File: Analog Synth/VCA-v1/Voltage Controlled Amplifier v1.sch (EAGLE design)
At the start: 40 parts, among them IC2 TL084P, IC3 TL084P, IC4 CA3046

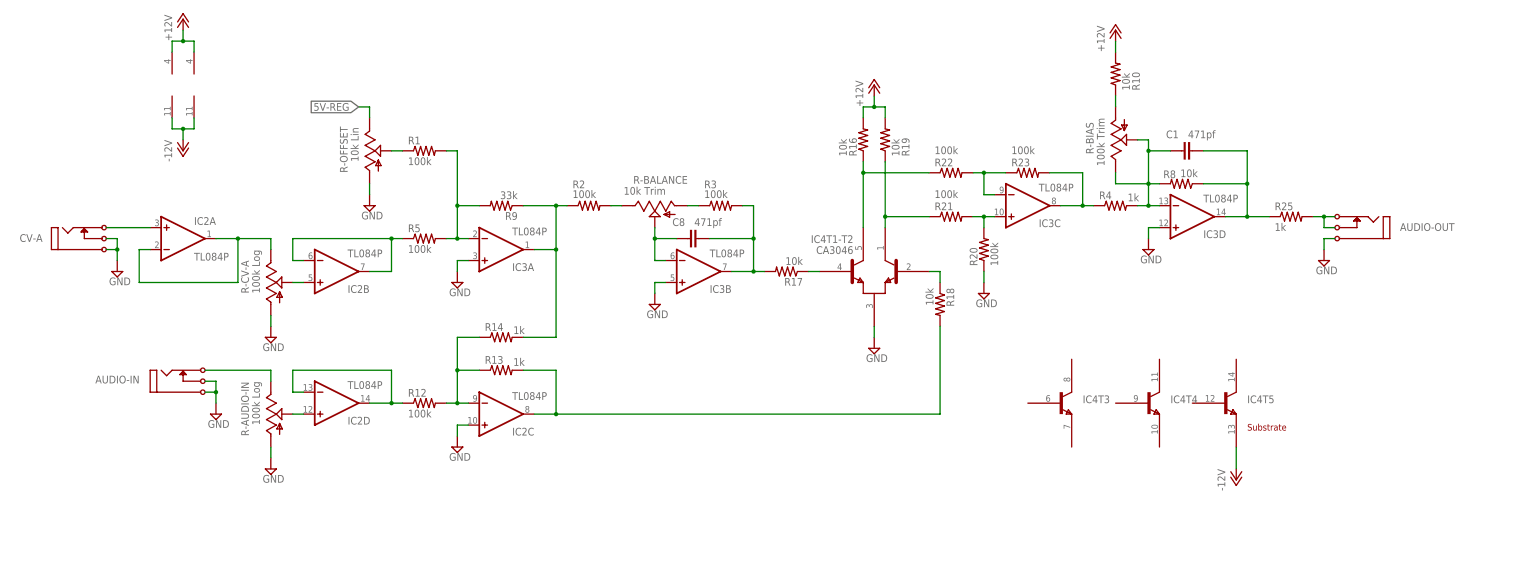
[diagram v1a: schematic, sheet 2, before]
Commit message: working on VCA more. added caps to filter RF by shunting high frequencies to ground.
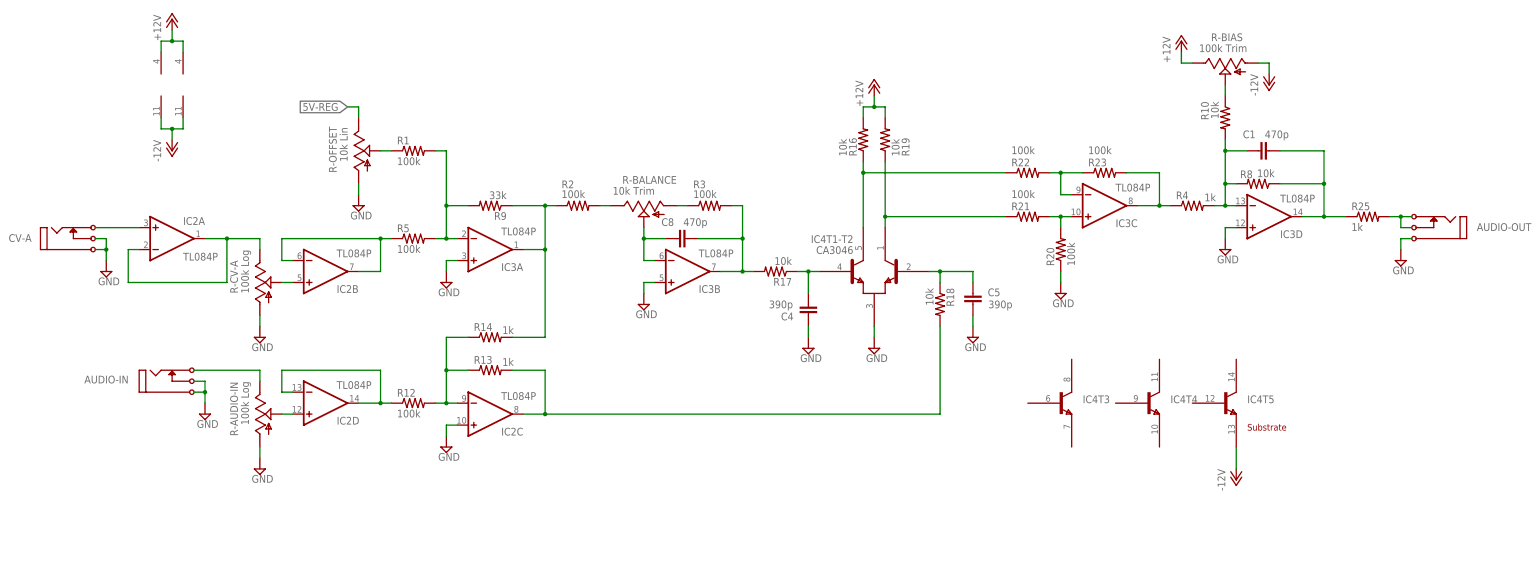
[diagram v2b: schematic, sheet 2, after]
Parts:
- added C4, C5: 390p, capacitor-wima:C2.5/2
- C1, C8: value 471pf -> 470p
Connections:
- removed net N$16: R-BIAS.A, R10.1
- new net N$11: R-BIAS.S, R10.1
- net +12V: now also R-BIAS.E; no longer R10.2
- net -12V: now also R-BIAS.A
- net GND: now also C4.1, C5.2
- net N$2: now also C4.2
- net N$20: now also R10.2; no longer R-BIAS.E, R-BIAS.S
- net N$21: now also C5.1
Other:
- moved on the sheet: AUDIO-IN, AUDIO-OUT, C1, C8, CV-A, IC2A, IC2B, IC2C, IC2D, IC3A, IC3B, IC3C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

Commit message: "Finished" VCA-v1. Ordered PCBs from dirtypcbs.com.
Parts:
- added C10: 10µ, rcl:C-US025-050X050
- added IC1: 79L05, linear:79L05Z
- added LED-CV: TLLG4400, led:TLLG4400
- added R15: 10k, resistor:R-US_0204/2V
- added R24: 22k, resistor:R-US_0204/2V
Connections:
- removed net 5V-REG: R-OFFSET.E
- new net -5V: C10.2, IC1.VO, LED-CV.C
- new net N$12: LED-CV.A, R15.1
- new net N$49: R-OFFSET.E, R24.1
- net +12V: now also R24.2
- net -12V: now also IC1.VI
- net GND: now also C10.1, IC1.GND
- net N$1: now also R15.2
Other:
- moved on the sheet: AUDIO-IN, IC2D, R-AUDIO-IN
